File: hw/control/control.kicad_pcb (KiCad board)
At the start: 2 copper layers, 200 x 100 mm, 141 parts, among them J101 Screw_Terminal_01x02, J102 Screw_Terminal_01x03, J103 Screw_Terminal_01x03, J301 Conn_02x05_Odd_Even, J302 Conn_01x04, J303 Raspberry_Pi_0_2_3, J304 Micro_SD_Card, J305 Conn_01x06, Q1001 BC807, Q1002 BC817, Q401 BC817, Q501 BC817, Q601 BC817, Q701 BC817, Q801 BC807, Q802 BC817, Q901 AOSP21357, Q902 IRF4905, U1001 LM2678T-ADJ, U1101 SN74AHCT125D, U201 LM2596T-ADJ, U801 LM2678T-ADJ

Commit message: [hw] Shrink the LED power supply layout
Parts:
- moved J102 53.8 mm to (185.0, 142.0)
- moved J103 53.8 mm to (201.8, 142.0)
- moved D201 39.3 mm to (-46.2, 57.3)
- moved D203 39.3 mm to (-46.1, 73.4)
- moved L201 39.3 mm to (-60.2, 45.3)
- moved C201 39.3 mm to (-55.0, 56.7)
- moved C203 39.3 mm to (-55.0, 61.6)
- moved C204 39.3 mm to (-36.4, 47.8)
- moved C205 39.3 mm to (-37.8, 59.3)
- moved D202 39.3 mm to (-45.6, 68.4)
- moved R202 39.3 mm to (-55.1, 64.6)
- moved U201 39.3 mm to (-66.6, 64.2)
- moved C202 39.3 mm to (-47.9, 48.8)
- moved C206 39.3 mm to (-50.2, 61.6)
- moved R201 39.3 mm to (-45.5, 61.6)
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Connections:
- J303 pad 27: (no net) -> Net-(J303-Pad27)
- J303 pad 28: (no net) -> Net-(J303-Pad28)
- J303 pad 29: (no net) -> Net-(J303-Pad29)
- J303 pad 31: (no net) -> Net-(J303-Pad31)
- J303 pad 35: (no net) -> Net-(J303-Pad35)
- J303 pad 36: (no net) -> Net-(J303-Pad36)
- J303 pad 40: (no net) -> Net-(J303-Pad40)
- J304 pad 1: (no net) -> Net-(J304-Pad1)
- J304 pad 8: (no net) -> Net-(J304-Pad8)
- U1001 pad 5: (no net) -> Net-(U1001-Pad5)
- U801 pad 5: (no net) -> Net-(U801-Pad5)
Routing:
- net /LED1 Power/ENABLE: track 37.0 -> 16.4 mm, vias 1 -> 0
- net /LED0 Power/ENABLE: track 37.0 -> 16.4 mm, vias 1 -> 0
- net Net-(Q1002-Pad1): track 9.06 -> 0.00 mm
- net Net-(Q802-Pad1): track 9.06 -> 0.00 mm
- net /LED1 Power/VOUT: track 0.00 -> 7.67 mm
- net /LED0 Power/VOUT: track 0.00 -> 7.67 mm
- net GND: track 6.70 -> 0.00 mm, vias 51 -> 41
- net +5V: track 5.54 -> 0.00 mm
- net Net-(C809-Pad2): track 28.8 -> 23.5 mm
- net Net-(C1009-Pad2): track 28.8 -> 23.5 mm
- net Net-(Q801-Pad1): track 5.02 -> 0.00 mm
- net Net-(Q1001-Pad1): track 5.02 -> 0.00 mm
- net Net-(Q802-Pad3): track 3.31 -> 0.00 mm
- net Net-(Q1002-Pad3): track 3.31 -> 0.00 mm
- net /LED_PWR_EN1: track 2.25 -> 0.00 mm
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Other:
- net class Raw Power: clearance 0.5 -> 0.6

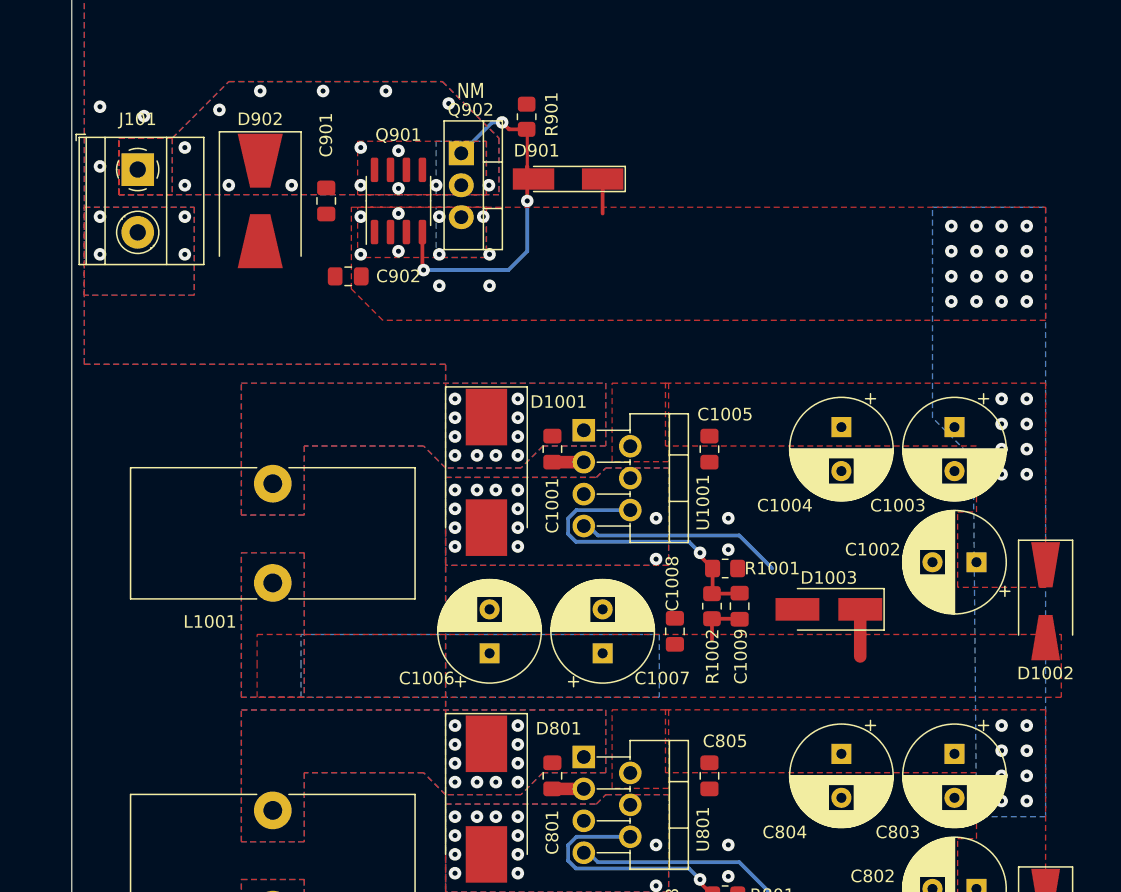
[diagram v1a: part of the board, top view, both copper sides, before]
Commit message: [hw] Optimize input protection layout
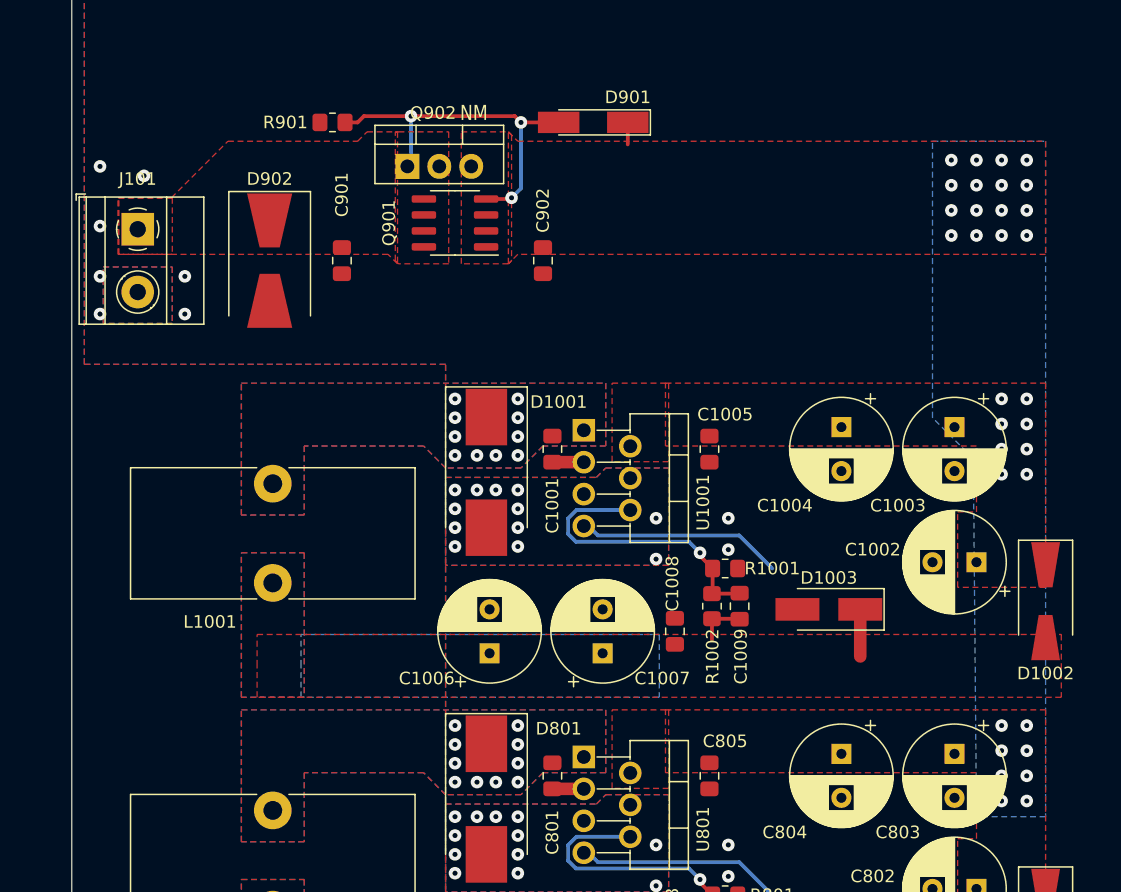
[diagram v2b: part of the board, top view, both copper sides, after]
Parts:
- moved C902 15.6 mm to (77.5, 86.8), turned to 270 degrees
- moved R901 15.5 mm to (60.8, 75.8), turned to 180 degrees
- moved D901 4.92 mm to (81.5, 75.8)
- moved C901 4.91 mm to (61.5, 86.8)
- moved Q901 4.83 mm to (70.5, 83.8), turned to 180 degrees
- moved D902 4.81 mm to (55.8, 86.8)
- moved J101 4.75 mm to (45.2, 84.2)
- moved Q902 4.41 mm to (66.7, 79.2), turned to 0 degrees
- moved g** 3.69 mm to (73.5, 75.0), turned to 180 degrees
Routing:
- net /LED0 Power/VIN: track 2.75 -> 1.75 mm, vias 42 -> 32
- net Net-(D901-Pad2): track 29.3 -> 29.9 mm
- net /Input Protection/V_A: vias 15 -> 0
- removed copper zone on B.Cu, net /Input Protection/V_A
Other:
- rule pad_to_mask_clearance: 0.05 -> 0.1

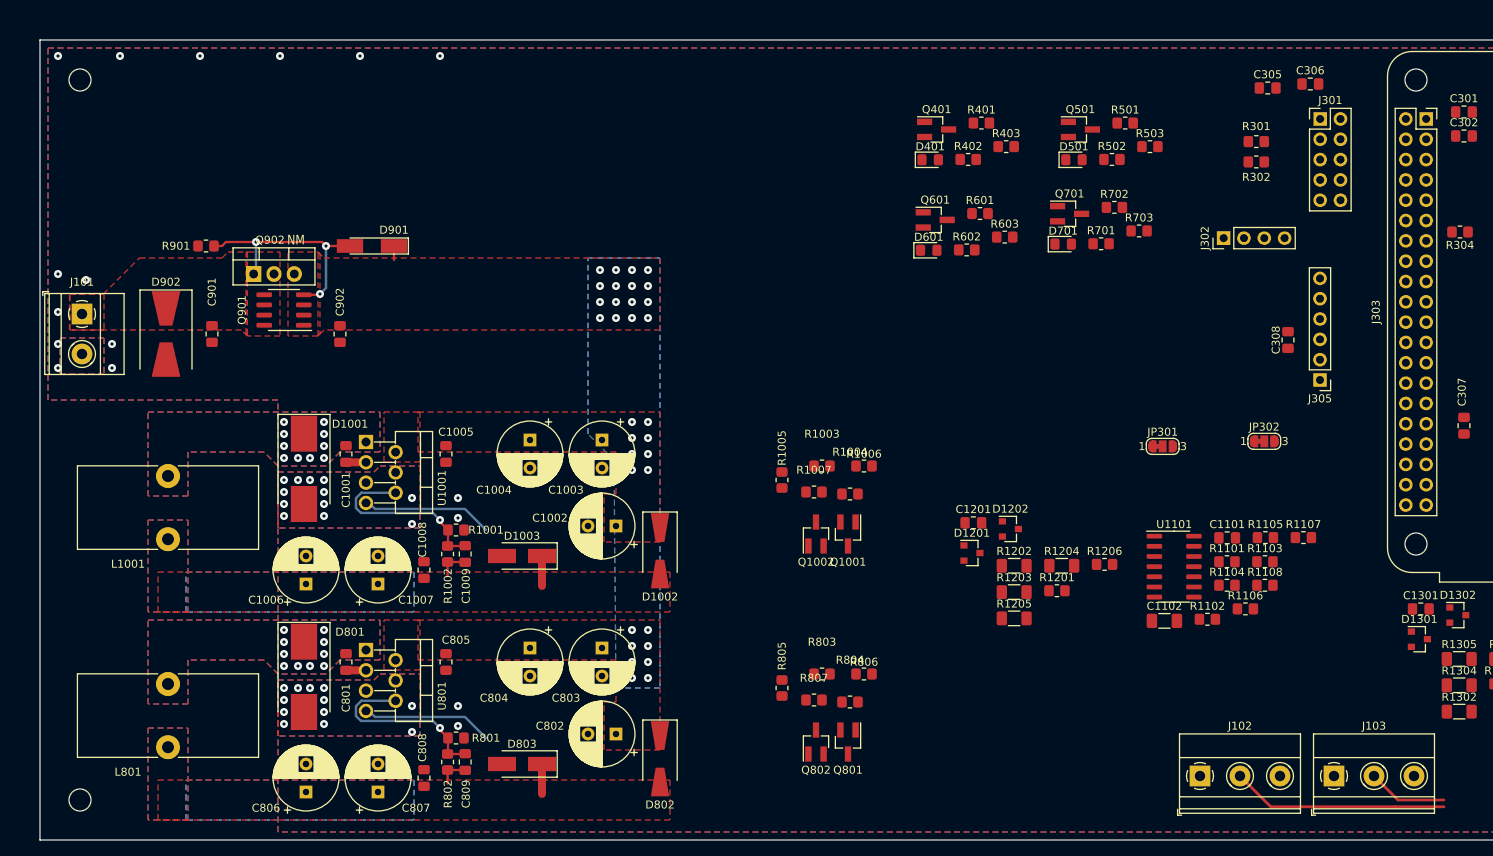
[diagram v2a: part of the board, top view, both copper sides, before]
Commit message: [hw] Update LED power supply
* Add 10 uF capacitors
* Add more space heat sinks
* Add thermal reliefs
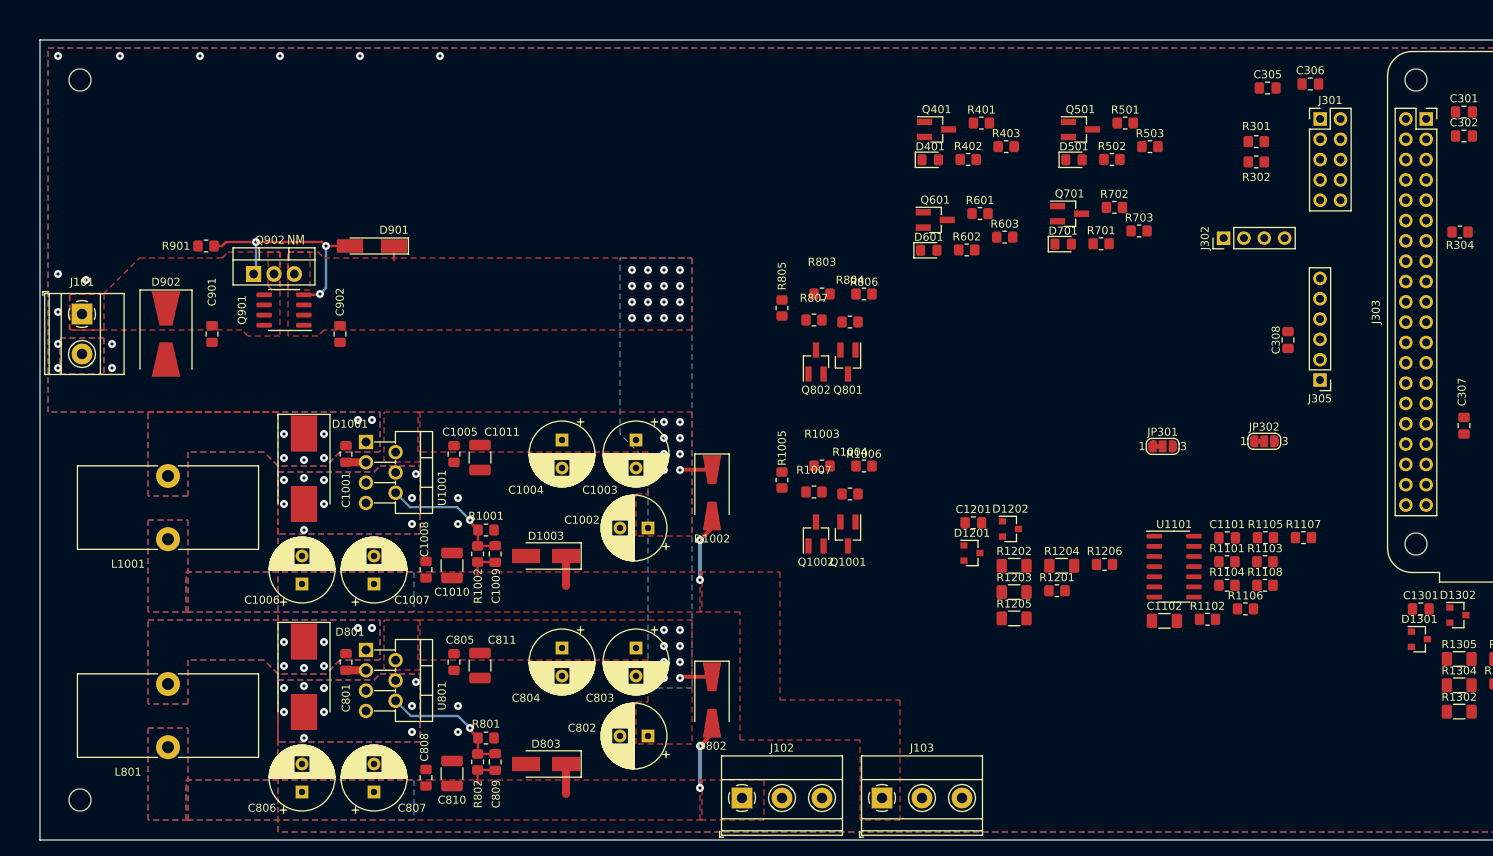
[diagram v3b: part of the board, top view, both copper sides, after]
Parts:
- added C1010: 10u, Capacitor_SMD:C_1210_3225Metric_Pad1.33x2.70mm_HandSolder, F.Cu at (91.5, 115.7)
- added C1011: 10u, Capacitor_SMD:C_1210_3225Metric_Pad1.33x2.70mm_HandSolder, F.Cu at (95.0, 102.2)
- added C810: 10u, Capacitor_SMD:C_1210_3225Metric_Pad1.33x2.70mm_HandSolder, F.Cu at (91.5, 141.7)
- added C811: 10u, Capacitor_SMD:C_1210_3225Metric_Pad1.33x2.70mm_HandSolder, F.Cu at (95.0, 128.2)
- moved J102 57.3 mm to (127.8, 144.8)
- moved J103 56.6 mm to (145.2, 144.8)
- moved Q801 47.5 mm to (141.0, 90.2)
- moved Q802 47.5 mm to (137.0, 90.2)
- moved R803 47.5 mm to (137.8, 81.8)
- moved R804 47.5 mm to (141.2, 85.2)
- moved R805 47.5 mm to (132.8, 83.5)
- moved R806 47.5 mm to (143.0, 81.8)
- moved R807 47.5 mm to (136.8, 85.0)
- moved D802 9.81 mm to (124.0, 132.5)
- moved D1002 9.74 mm to (124.0, 106.6)
- moved C1003 4.25 mm to (114.5, 100.0)
- moved C803 4.25 mm to (114.5, 126.0)
- moved C1002 4.01 mm to (116.0, 111.0)
- moved C802 4.01 mm to (116.0, 137.0)
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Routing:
- net /LED Driver/DATA_OUT0: track 27.1 -> 0.00 mm
- net /LED1 Power/ENABLE: track 16.4 -> 0.00 mm
- net /LED0 Power/ENABLE: track 16.4 -> 0.00 mm
- net /LED Driver/DATA_OUT1: track 9.99 -> 0.00 mm
- net /LED0 Power/VOUT: track 7.67 -> 16.4 mm, vias 0 -> 2
- net /LED1 Power/VOUT: track 7.67 -> 16.3 mm, vias 0 -> 2
- net /LED0 Power/VIN: track 1.75 -> 9.83 mm
- net Net-(C809-Pad2): track 23.5 -> 16.6 mm
- net Net-(C1009-Pad2): track 23.5 -> 16.6 mm
- net Net-(C801-Pad1): vias 10 -> 7
- net Net-(C1001-Pad1): vias 10 -> 7
- net GND: vias 41 -> 35

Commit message: [hw] Add 5V supply layout
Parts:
- removed R401, R501, R601, R701: 330R, Resistor_SMD:R_0805_2012Metric_Pad1.20x1.40mm_HandSolder
- added C207: 10u, Capacitor_SMD:C_1210_3225Metric_Pad1.33x2.70mm_HandSolder, F.Cu at (94.0, 60.8)
- added C208: 10u, Capacitor_SMD:C_1210_3225Metric_Pad1.33x2.70mm_HandSolder, F.Cu at (94.0, 54.2)
- moved D203 175.5 mm to (128.5, 55.0)
- moved D202 161.7 mm to (116.0, 64.2)
- moved C201 155.6 mm to (100.5, 55.3), turned to 90 degrees
- moved C204 155.3 mm to (118.8, 54.5), turned to 270 degrees
- moved R202 154.5 mm to (99.2, 58.2)
- moved U201 154.1 mm to (87.5, 62.2), turned to 90 degrees
- moved C202 151.5 mm to (102.5, 67.0), turned to 90 degrees
- moved C205 147.4 mm to (109.5, 54.5), turned to 270 degrees
- moved C203 146.1 mm to (91.0, 61.2), turned to 90 degrees
- moved R201 143.8 mm to (98.2, 55.2), turned to 90 degrees
- moved C206 141.5 mm to (91.0, 53.7), turned to 270 degrees
- moved D201 120.7 mm to (74.5, 58.5), turned to 90 degrees
- moved L201 120.6 mm to (59.2, 62.0), turned to 180 degrees
- moved Q801 73.6 mm to (195.2, 140.0)
- moved Q802 73.6 mm to (191.2, 140.0)
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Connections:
- J303 pad 27: Net-(J303-Pad27) -> (no net)
- J303 pad 28: Net-(J303-Pad28) -> (no net)
- J303 pad 29: Net-(J303-Pad29) -> (no net)
- J303 pad 31: Net-(J303-Pad31) -> (no net)
- J303 pad 35: Net-(J303-Pad35) -> (no net)
- J303 pad 36: Net-(J303-Pad36) -> (no net)
- J303 pad 40: Net-(J303-Pad40) -> (no net)
- J304 pad 1: Net-(J304-Pad1) -> (no net)
- J304 pad 8: Net-(J304-Pad8) -> (no net)
- U1001 pad 5: Net-(U1001-Pad5) -> (no net)
- U801 pad 5: Net-(U801-Pad5) -> (no net)
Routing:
- net /LED1 Power/ENABLE: track 0.00 -> 114.3 mm, vias 0 -> 1
- net /LED0 Power/ENABLE: track 0.00 -> 98.0 mm, vias 0 -> 1
- net +5V: track 0.00 -> 41.6 mm
- net /LED Driver/DATA_OUT0: track 0.00 -> 34.9 mm
- net /LED0 Power/VIN: track 9.83 -> 39.4 mm
- net Net-(C201-Pad1): track 0.00 -> 23.0 mm
- net /LED Driver/DATA_OUT1: track 0.00 -> 16.7 mm
- net Net-(D201-Pad1): track 0.00 -> 13.4 mm, vias 0 -> 3
- net Net-(Q701-Pad3): track 0.00 -> 2.66 mm
- net Net-(Q601-Pad3): track 0.00 -> 2.66 mm
- net Net-(Q501-Pad3): track 0.00 -> 2.66 mm
- net Net-(Q401-Pad3): track 0.00 -> 2.66 mm
- net Net-(D701-Pad1): track 0.00 -> 2.39 mm
- net Net-(D601-Pad1): track 0.00 -> 2.39 mm
- net Net-(D501-Pad1): track 0.00 -> 2.39 mm
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- added copper zone on F.Cu, net +5V
- added copper zone on F.Cu, net Net-(D201-Pad1)
